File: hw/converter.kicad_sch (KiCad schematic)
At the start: 15 parts, among them J301 1935776, J302 1935776, Q301 SW_L, Q302 SW_H

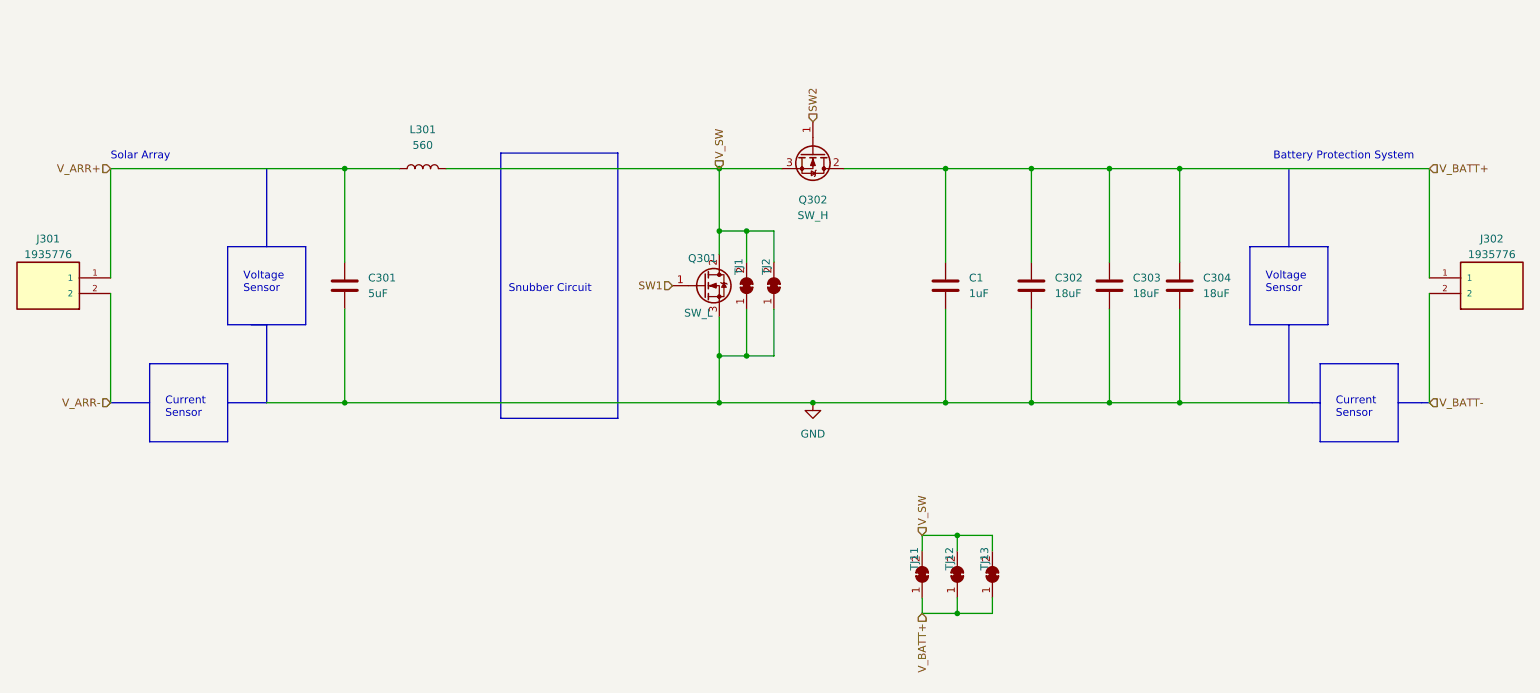
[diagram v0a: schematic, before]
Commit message: segregating code into design procedures
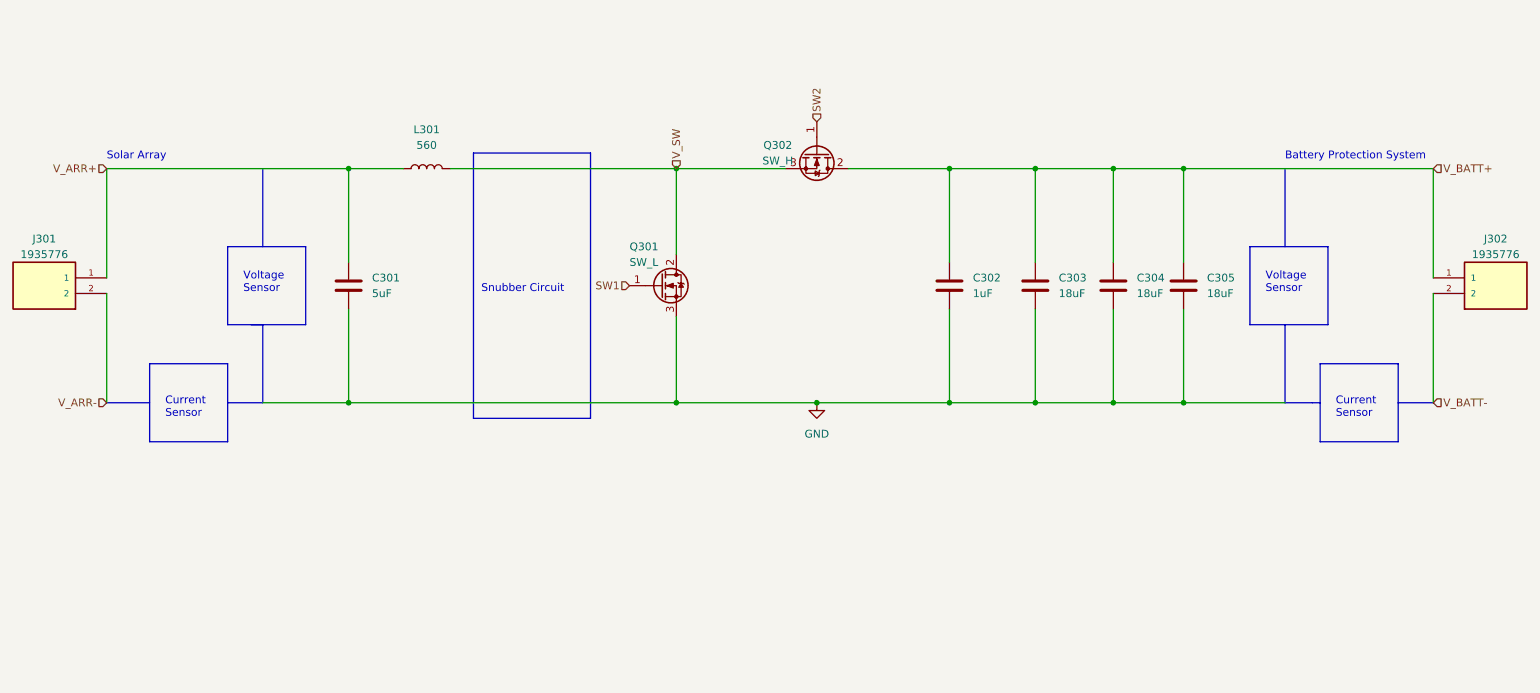
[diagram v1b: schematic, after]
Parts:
- removed TJ1, TJ11, TJ12, TJ13, TJ2: Thermal Jumper, Resistor_SMD:R_0805_2012Metric, symbol Jumper:SolderJumper_2_Bridged
- renumbered C1 to C302, C302 to C303, C303 to C304, C304 to C305
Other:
- moved on the sheet: C301, C302, C303, C304, C305, J301, J302, L301, Q301, Q302

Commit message: Design partioning, might've gotten the parameters down, more documents
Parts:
- removed L301: 560, mppt:B65812N1005D002, symbol Device:L
- added HS301: Heatsink_Pad, mppt:WayinTop_HS, symbol Mechanical:Heatsink
- added L301: B65878E1012D001, mppt:B65878E1012D001, symbol B65878E1012D001:B65878E1012D001
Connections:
- net V_ARR+: now also L301.A
- net V_SW: now also L301.B
- no-connect marks 0 -> 12
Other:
- note removed: "Snubber Circuit"
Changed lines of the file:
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@@
   (junction (at 191.77 109.22) (diameter 0) (color 0 0 0 0)
   )
+  (junction (at 215.9 109.22) (diameter 0) (color 0 0 0 0)
+  )
+  (junction (at 80.01 109.22) (diameter 0) (color 0 0 0 0)
+  )
+  (junction (at 204.47 71.12) (diameter 0) (color 0 0 0 0)
+  )
+  (junction (at 215.9 71.12) (diameter 0) (color 0 0 0 0)
+  )
+  (junction (at 204.47 109.22) (diameter 0) (color 0 0 0 0)
+  )
+  (junction (at 177.8 71.12) (diameter 0) (color 0 0 0 0)
+  )
+  (junction (at 133.35 71.12) (diameter 0) (color 0 0 0 0)
+  )
+  (junction (at 133.35 109.22) (diameter 0) (color 0 0 0 0)
+  )
+  (junction (at 191.77 71.12) (diameter 0) (color 0 0 0 0)
+  )
   (junction (at 80.01 71.12) (diameter 0) (color 0 0 0 0)
   )
-  (junction (at 215.9 109.22) (diameter 0) (color 0 0 0 0)
-  )
-  (junction (at 80.01 109.22) (diameter 0) (color 0 0 0 0)
-  )
-  (junction (at 204.47 71.12) (diameter 0) (color 0 0 0 0)
-  )
-  (junction (at 215.9 71.12) (diameter 0) (color 0 0 0 0)
-  )
-  (junction (at 204.47 109.22) (diameter 0) (color 0 0 0 0)
-  )
-  (junction (at 177.8 71.12) (diameter 0) (color 0 0 0 0)
-  )
-  (junction (at 133.35 109.22) (diameter 0) (color 0 0 0 0)
-  )
-  (junction (at 191.77 71.12) (diameter 0) (color 0 0 0 0)
-  )
-  (junction (at 133.35 71.12) (diameter 0) (color 0 0 0 0)
-  )
   (junction (at 156.21 109.22) (diameter 0) (color 0 0 0 0)
   )
   (junction (at 177.8 109.22) (diameter 0) (color 0 0 0 0)
   )
+  (no_connect (at 95.25 63.5))
+  (no_connect (at 118.11 63.5))
+  (no_connect (at 95.25 60.96))
+  (no_connect (at 118.11 53.34))
+  (no_connect (at 118.11 58.42))
+  (no_connect (at 95.25 53.34))
+  (no_connect (at 95.25 58.42))
+  (no_connect (at 118.11 66.04))
+  (no_connect (at 95.25 55.88))
+  (no_connect (at 118.11 60.96))
+  (no_connect (at 118.11 55.88))
+  (no_connect (at 95.25 66.04))
   (polyline (pts (xy 66.04 71.12) (xy 66.04 83.82))
     (stroke (width 0) (type default))
@@
     (stroke (width 0) (type default))
   )
+  (wire (pts (xy 115.57 71.12) (xy 133.35 71.12))
+    (stroke (width 0) (type default))
+  )
   (wire (pts (xy 40.64 91.44) (xy 40.64 109.22))
     (stroke (width 0) (type default))
@@
     (stroke (width 0) (type default))
   )
-  (polyline (pts (xy 119.38 111.76) (xy 100.33 111.76))
-    (stroke (width 0) (type default))
-  )
   (polyline (pts (xy 236.855 109.22) (xy 238.125 109.22))
     (stroke (width 0) (type default))
@@
     (stroke (width 0) (type default))
   )
+  (wire (pts (xy 80.01 71.12) (xy 97.79 71.12))
+    (stroke (width 0) (type default))
+  )
   (polyline (pts (xy 238.125 102.87) (xy 238.125 115.57))
     (stroke (width 0) (type default))
@@
     (stroke (width 0) (type default))
   )
-  (wire (pts (xy 96.52 71.12) (xy 133.35 71.12))
-    (stroke (width 0) (type default))
-  )
   (wire (pts (xy 156.21 109.22) (xy 177.8 109.22))
     (stroke (width 0) (type default))
@@
     (stroke (width 0) (type default))
   )
-  (wire (pts (xy 80.01 71.12) (xy 88.9 71.12))
-    (stroke (width 0) (type default))
-  )
-  (polyline (pts (xy 119.38 68.58) (xy 119.38 111.76))
-    (stroke (width 0) (type default))
-  )
   (polyline (pts (xy 73.025 96.52) (xy 60.325 96.52))
     (stroke (width 0) (type default))
@@
     (stroke (width 0) (type default))
   )
-  (polyline (pts (xy 100.33 68.58) (xy 119.38 68.58))
-    (stroke (width 0) (type default))
-  )
   (polyline (pts (xy 232.41 71.12) (xy 232.41 83.82))
     (stroke (width 0) (type default))
@@
     (stroke (width 0) (type default))
   )
-  (polyline (pts (xy 100.33 68.58) (xy 100.33 111.76))
-    (stroke (width 0) (type default))
-  )
   (wire (pts (xy 256.54 71.12) (xy 256.54 88.9))
     (stroke (width 0) (type default))
   )
   (text "Battery Protection System\n" (at 232.41 69.85 0)
-    (effects (font (size 1.27 1.27)) (justify left bottom))
-  )
-  (text "Snubber Circuit" (at 101.6 91.44 0)
     (effects (font (size 1.27 1.27)) (justify left bottom))
   )
@@
     )
   )
+  (symbol (lib_id "Mechanical:Heatsink") (at 133.35 52.07 0) (unit 1)
+    (in_bom yes) (on_board yes) (dnp no) (fields_autoplaced)
+    (property "Reference" "HS301" (at 137.16 50.8 0)
+      (effects (font (size 1.27 1.27)) (justify left))
+    )
+    (property "Value" "Heatsink_Pad" (at 137.16 53.34 0)
+      (effects (font (size 1.27 1.27)) (justify left))
+    )
+    (property "Footprint" "mppt:WayinTop_HS" (at 133.6548 52.07 0)
+      (effects (font (size 1.27 1.27)) hide)
+    )
+    (property "Datasheet" "~" (at 133.6548 52.07 0)
+      (effects (font (size 1.27 1.27)) hide)
+    )
+    (instances
+      (project "mppt"
+        (path "/06fd3a42-664d-41bc-bf0f-b5ee0ddcc902/9cd55a57-0ec8-481d-b571-b5fdbe353ce7"
+          (reference "HS301") (unit 1)
+        )
+      )
+    )
+  )
   (symbol (lib_id "Device:C") (at 204.47 90.17 0) (unit 1)
     (in_bom yes) (on_board yes) (dnp no)
@@
     )
   )
-  (symbol (lib_id "Device:L") (at 92.71 71.12 90) (unit 1)
-    (in_bom yes) (on_board yes) (dnp no) (fields_autoplaced)
-    (property "Reference" "L301" (at 92.71 64.77 90)
-      (effects (font (size 1.27 1.27)))
-    )
-    (property "Value" "560" (at 92.71 67.31 90)
-      (effects (font (size 1.27 1.27)))
-    )
-    (property "Footprint" "mppt:B65812N1005D002" (at 92.71 71.12 0)
-      (effects (font (size 1.27 1.27)) hide)
-    )
-    (property "Datasheet" "https://product.tdk.com/system/files/dam/doc/product/ferrite/ferrite/ferrite-acc/data_sheet/80/db/fer/rm_8.pdf" (at 92.71 71.12 0)
-      (effects (font (size 1.27 1.27)) hide)
-    )
-    (pin "1")
-    (pin "2")
-    (instances
-      (project "mppt"
-        (path "/06fd3a42-664d-41bc-bf0f-b5ee0ddcc902/9cd55a57-0ec8-481d-b571-b5fdbe353ce7"
-          (reference "L301") (unit 1)
-        )
-      )
-    )
-  )
   (symbol (lib_id "Device:C") (at 80.01 90.17 0) (unit 1)
     (in_bom yes) (on_board yes) (dnp no) (fields_autoplaced)
@@
         )
       )
+    )
+  )
+  (symbol (lib_id "B65878E1012D001:B65878E1012D001") (at 95.25 53.34 0) (unit 1)
+    (in_bom yes) (on_board yes) (dnp no) (fields_autoplaced)
+    (property "Reference" "L301" (at 106.68 46.99 0)
+      (effects (font (size 1.27 1.27)))
+    )
+    (property "Value" "B65878E1012D001" (at 106.68 49.53 0)
+      (effects (font (size 1.27 1.27)))
+    )
+    (property "Footprint" "mppt:B65878E1012D001" (at 114.3 50.8 0)
+      (effects (font (size 1.27 1.27)) (justify left) hide)
+    )
+    (property "Datasheet" "https://product.tdk.com/system/files/dam/doc/product/ferrite/ferrite/ferrite-acc/data_sheet/80/db/fer/b65877a.pdf" (at 114.3 53.34 0)
+      (effects (font (size 1.27 1.27)) (justify left) hide)
+    )
+    (property "Description" "Ferrite Accessories, PQ Cores Accessories, Coil former (PQ 26/25)" (at 114.3 55.88 0)
+      (effects (font (size 1.27 1.27)) (justify left) hide)
+    )
+    (property "Height" "29.3" (at 114.3 58.42 0)
+      (effects (font (size 1.27 1.27)) (justify left) hide)
+    )
+    (property "Mouser Part Number" "871-B65878E1012D001" (at 114.3 60.96 0)
+      (effects (font (size 1.27 1.27)) (justify left) hide)
+    )
+    (property "Mouser Price/Stock" "https://www.mouser.co.uk/ProductDetail/EPCOS-TDK/B65878E1012D001?qs=rRTa3HiPCWMeN2nCnqHv0g%3D%3D" (at 114.3 63.5 0)
+      (effects (font (size 1.27 1.27)) (justify left) hide)
+    )
+    (property "Manufacturer_Name" "TDK" (at 114.3 66.04 0)
+      (effects (font (size 1.27 1.27)) (justify left) hide)
+    )
+    (property "Manufacturer_Part_Number" "B65878E1012D001" (at 114.3 68.58 0)
+      (effects (font (size 1.27 1.27)) (justify left) hide)
+    )
+    (pin "1")
+    (pin "10")
+    (pin "11")
+    (pin "12")
+    (pin "2")
+    (pin "3")
+    (pin "4")
+    (pin "5")
+    (pin "6")
+    (pin "7")
+    (pin "8")
+    (pin "9")
+    (pin "A")
+    (pin "B")
+    (instances
+      (project "mppt"
+        (path "/06fd3a42-664d-41bc-bf0f-b5ee0ddcc902/9cd55a57-0ec8-481d-b571-b5fdbe353ce7"
+          (reference "L301") (unit 1)
+        )
+      )

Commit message: added Vsw test point and altered Vsw trace slightly
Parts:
- added TP407: V_SW, TestPoint:TestPoint_Pad_1.0x1.0mm, symbol Connector:TestPoint
- added TP407: GND, TestPoint:TestPoint_Pad_1.0x1.0mm, symbol Connector:TestPoint
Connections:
- net GND: now also TP407.1
- net V_SW: now also TP407.1
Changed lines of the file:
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@@
   (junction (at 177.8 71.12) (diameter 0) (color 0 0 0 0)
   )
+  (junction (at 133.35 98.425) (diameter 0) (color 0 0 0 0)
+  )
   (junction (at 133.35 71.12) (diameter 0) (color 0 0 0 0)
+  )
+  (junction (at 133.35 81.28) (diameter 0) (color 0 0 0 0)
   )
   (junction (at 133.35 109.22) (diameter 0) (color 0 0 0 0)
@@
     (stroke (width 0) (type default))
   )
-  (wire (pts (xy 133.35 95.25) (xy 133.35 109.22))
+  (wire (pts (xy 133.35 95.25) (xy 133.35 98.425))
     (stroke (width 0) (type default))
   )
@@
     (stroke (width 0) (type default))
   )
-  (wire (pts (xy 133.35 71.12) (xy 133.35 85.09))
+  (wire (pts (xy 133.35 71.12) (xy 133.35 81.28))
     (stroke (width 0) (type default))
   )
@@
     (stroke (width 0) (type default))
   )
+  (wire (pts (xy 133.35 98.425) (xy 133.35 109.22))
+    (stroke (width 0) (type default))
+  )
   (polyline (pts (xy 238.125 102.87) (xy 238.125 115.57))
     (stroke (width 0) (type default))
@@
   )
   (wire (pts (xy 40.64 88.9) (xy 40.64 71.12))
+    (stroke (width 0) (type default))
+  )
+  (wire (pts (xy 133.35 81.28) (xy 133.35 85.09))
     (stroke (width 0) (type default))
   )
@@
     )
   )
+  (symbol (lib_id "Connector:TestPoint") (at 133.35 81.28 270) (mirror x) (unit 1)
+    (in_bom yes) (on_board yes) (dnp no)
+    (property "Reference" "TP407" (at 139.7 81.28 0)
+      (effects (font (size 1 1)) (justify bottom))
+    )
+    (property "Value" "V_SW" (at 138.43 81.28 0)
+      (effects (font (size 1 1)))
+    )
+    (property "Footprint" "TestPoint:TestPoint_Pad_1.0x1.0mm" (at 133.35 81.28 0)
+      (effects (font (size 1 1)) hide)
+    )
+    (property "Datasheet" "" (at 133.35 81.28 0)
+      (effects (font (size 1 1)) hide)
+    )
+    (pin "1")
+    (instances
+      (project "mppt"
+        (path "/06fd3a42-664d-41bc-bf0f-b5ee0ddcc902/92f2c78d-fd2c-4f90-b3c1-261313d81f32"
+          (reference "TP407") (unit 1)
+        )
+        (path "/06fd3a42-664d-41bc-bf0f-b5ee0ddcc902/9cd55a57-0ec8-481d-b571-b5fdbe353ce7"
+          (reference "TP1") (unit 1)
+        )
+      )
+      (project "MPPT"
+        (path "/bb6fe1c9-daf9-447c-ad0c-700b5a8127f9/57cacabc-73fb-43df-b057-ebb178f994df"
+          (reference "TP504") (unit 1)
+        )
+      )
+    )
+  )
   (symbol (lib_id "1935776:1935776") (at 256.54 88.9 0) (unit 1)
     (in_bom yes) (on_board yes) (dnp no)
@@
         )
       )
+    )
+  )
+  (symbol (lib_id "Connector:TestPoint") (at 133.35 98.425 270) (mirror x) (unit 1)
+    (in_bom yes) (on_board yes) (dnp no)
+    (property "Reference" "TP407" (at 139.7 98.425 0)
+      (effects (font (size 1 1)) (justify bottom))
+    )
+    (property "Value" "GND" (at 138.43 98.425 0)
+      (effects (font (size 1 1)))
+    )
+    (property "Footprint" "TestPoint:TestPoint_Pad_1.0x1.0mm" (at 133.35 98.425 0)
+      (effects (font (size 1 1)) hide)
+    )
+    (property "Datasheet" "" (at 133.35 98.425 0)
+      (effects (font (size 1 1)) hide)
+    )
+    (pin "1")
+    (instances
+      (project "mppt"
+        (path "/06fd3a42-664d-41bc-bf0f-b5ee0ddcc902/92f2c78d-fd2c-4f90-b3c1-261313d81f32"
+          (reference "TP407") (unit 1)
+        )
+        (path "/06fd3a42-664d-41bc-bf0f-b5ee0ddcc902/9cd55a57-0ec8-481d-b571-b5fdbe353ce7"
+          (reference "TP2") (unit 1)
+        )
+      )
+      (project "MPPT"
+        (path "/bb6fe1c9-daf9-447c-ad0c-700b5a8127f9/57cacabc-73fb-43df-b057-ebb178f994df"
+          (reference "TP504") (unit 1)
+        )
+      )

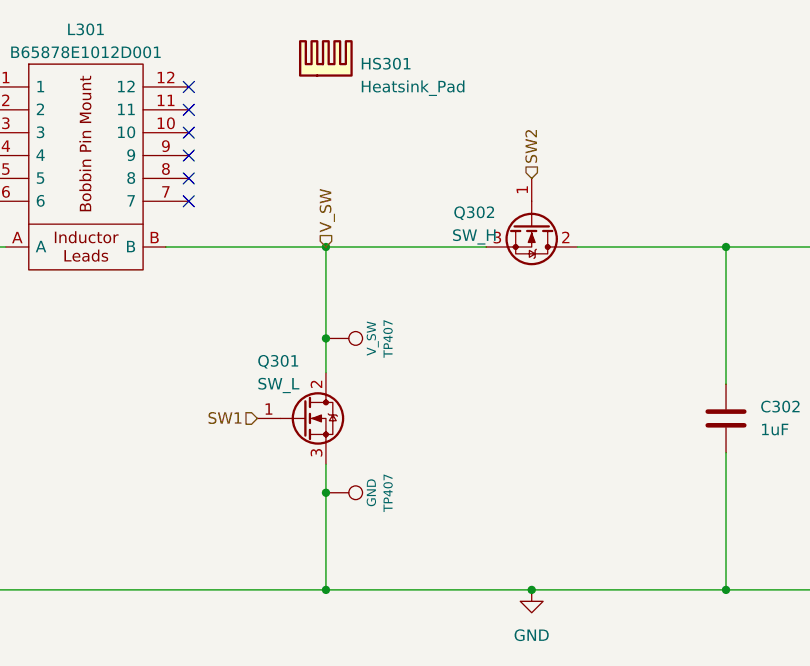
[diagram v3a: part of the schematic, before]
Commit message: Added proper signal TPs for Vsw, both gate signals, and PWM, added BNC connector for PWM control signal to STM analog pin, increased Vsw zone on F.cu, in.1, and in.2, reduced vias directly under fets, changed heatsink holesto pads for proper zone margins
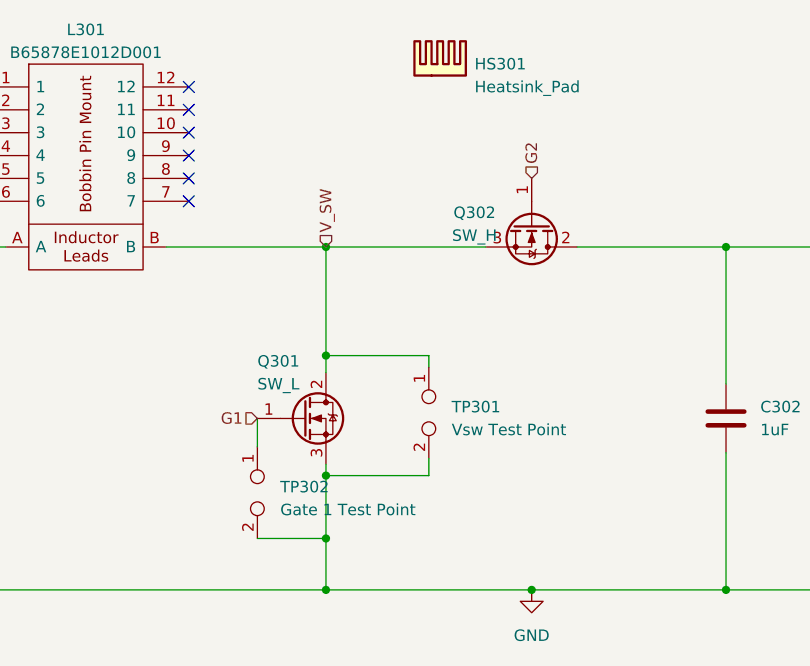
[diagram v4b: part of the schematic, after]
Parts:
- removed TP407: V_SW, TestPoint:TestPoint_Pad_1.0x1.0mm, symbol Connector:TestPoint
- removed TP407: GND, TestPoint:TestPoint_Pad_1.0x1.0mm, symbol Connector:TestPoint
- added TP301: Vsw Test Point, mppt:SignalTP, symbol Connector:TestPoint_2Pole
- added TP302: Gate 1 Test Point, mppt:SignalTP, symbol Connector:TestPoint_2Pole
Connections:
- net GND: now also TP301.2, TP302.2
- net V_SW: now also TP301.1
- net SW1 renamed G1
- net G1: now also TP302.1
- net SW2 renamed G2
